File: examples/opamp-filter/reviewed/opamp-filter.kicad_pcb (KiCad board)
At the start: 2 copper layers, 80 x 45 mm, 19 parts, among them J1 IN, J2 5V, J3 OUT, U1 MCP6001R, U2 MCP6001R

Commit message: Regenerate the five with stitched pours, silk that speaks, and wires that never double back
All ten variants rebuilt by the fixed generator: reviewed boards carry
ground on both faces with the stitching ring (buck 35 vias, fpga 116),
thru_hole_only front pours, the board id and connector pin names in
silk, and the buck's explicit ground return; the sheets hook power up
through upright symbols and source-anchored flags with no overlapping
wires and no junction-less tees left. Every reviewed variant passes its
own gate with zero errors; every as-generated variant still fails, now
also for the rules this round added.

Co-Authored-By: Claude Fable 5 <noreply@anthropic.com>
Claude-Session: https://claude.ai/code/session_01DUj7Ltu92tWg159mCSacwY
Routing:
- net GND: vias 11 -> 33
- added copper zone on F.Cu, net GND
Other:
- board text added: "+5V"
- board text added: "GND"
- board text added: "IN"
- board text added: "OUT_AC"
- board text added: "opamp-filter rev A"
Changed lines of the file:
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@@
 	(via (at 154.0 76.6) (size 0.8) (drill 0.4) (layers "F.Cu" "B.Cu") (net 1))
 	(via (at 158.0 91.75) (size 0.8) (drill 0.4) (layers "F.Cu" "B.Cu") (net 1))
+	(via (at 104.5 64.5) (size 0.8) (drill 0.4) (layers "F.Cu" "B.Cu") (net 1))
+	(via (at 104.5 100.5) (size 0.8) (drill 0.4) (layers "F.Cu" "B.Cu") (net 1))
+	(via (at 114.5 64.5) (size 0.8) (drill 0.4) (layers "F.Cu" "B.Cu") (net 1))
+	(via (at 114.5 100.5) (size 0.8) (drill 0.4) (layers "F.Cu" "B.Cu") (net 1))
+	(via (at 124.5 64.5) (size 0.8) (drill 0.4) (layers "F.Cu" "B.Cu") (net 1))
+	(via (at 124.5 100.5) (size 0.8) (drill 0.4) (layers "F.Cu" "B.Cu") (net 1))
+	(via (at 134.5 64.5) (size 0.8) (drill 0.4) (layers "F.Cu" "B.Cu") (net 1))
+	(via (at 134.5 100.5) (size 0.8) (drill 0.4) (layers "F.Cu" "B.Cu") (net 1))
+	(via (at 144.5 64.5) (size 0.8) (drill 0.4) (layers "F.Cu" "B.Cu") (net 1))
+	(via (at 144.5 100.5) (size 0.8) (drill 0.4) (layers "F.Cu" "B.Cu") (net 1))
+	(via (at 154.5 64.5) (size 0.8) (drill 0.4) (layers "F.Cu" "B.Cu") (net 1))
+	(via (at 154.5 100.5) (size 0.8) (drill 0.4) (layers "F.Cu" "B.Cu") (net 1))
+	(via (at 164.5 64.5) (size 0.8) (drill 0.4) (layers "F.Cu" "B.Cu") (net 1))
+	(via (at 164.5 100.5) (size 0.8) (drill 0.4) (layers "F.Cu" "B.Cu") (net 1))
+	(via (at 174.5 64.5) (size 0.8) (drill 0.4) (layers "F.Cu" "B.Cu") (net 1))
+	(via (at 174.5 100.5) (size 0.8) (drill 0.4) (layers "F.Cu" "B.Cu") (net 1))
+	(via (at 104.5 74.5) (size 0.8) (drill 0.4) (layers "F.Cu" "B.Cu") (net 1))
+	(via (at 175.5 74.5) (size 0.8) (drill 0.4) (layers "F.Cu" "B.Cu") (net 1))
+	(via (at 104.5 84.5) (size 0.8) (drill 0.4) (layers "F.Cu" "B.Cu") (net 1))
+	(via (at 175.5 84.5) (size 0.8) (drill 0.4) (layers "F.Cu" "B.Cu") (net 1))
+	(via (at 104.5 94.5) (size 0.8) (drill 0.4) (layers "F.Cu" "B.Cu") (net 1))
+	(via (at 175.5 94.5) (size 0.8) (drill 0.4) (layers "F.Cu" "B.Cu") (net 1))
 	(zone
 		(net 1)
@@
 		(polygon (pts (xy 103.0 63.0) (xy 177.0 63.0) (xy 177.0 102.0) (xy 103.0 102.0)))
 	)
+	(zone
+		(net 1)
+		(net_name "GND")
+		(layer "F.Cu")
+		(hatch edge 0.5)
+		(connect_pads thru_hole_only
+			(clearance 0.4)
+		)
+		(min_thickness 0.175)
+		(filled_areas_thickness no)
+		(fill yes
+			(thermal_gap 0.5)
+			(thermal_bridge_width 0.5)
+		)
+		(polygon (pts (xy 103.0 63.0) (xy 177.0 63.0) (xy 177.0 102.0) (xy 103.0 102.0)))
+	)
+	(gr_text "opamp-filter rev A" (at 140.0 102.8 0) (layer "F.SilkS") (effects (font (size 1.0 1.0) (thickness 0.15))))
+	(gr_text "IN" (at 111.37 78.0 0) (layer "F.SilkS") (effects (font (size 0.8 0.8) (thickness 0.12))))
+	(gr_text "GND" (at 111.37 80.54 0) (layer "F.SilkS") (effects (font (size 0.8 0.8) (thickness 0.12))))
+	(gr_text "OUT_AC" (at 168.63 78.0 0) (layer "F.SilkS") (effects (font (size 0.8 0.8) (thickness 0.12))))
+	(gr_text "GND" (at 168.63 80.54 0) (layer "F.SilkS") (effects (font (size 0.8 0.8) (thickness 0.12))))
+	(gr_text "+5V" (at 170.0 74.3 0) (layer "F.SilkS") (effects (font (size 0.8 0.8) (thickness 0.12))))
+	(gr_text "GND" (at 175.0 74.3 0) (layer "F.SilkS") (effects (font (size 0.8 0.8) (thickness 0.12))))
 )

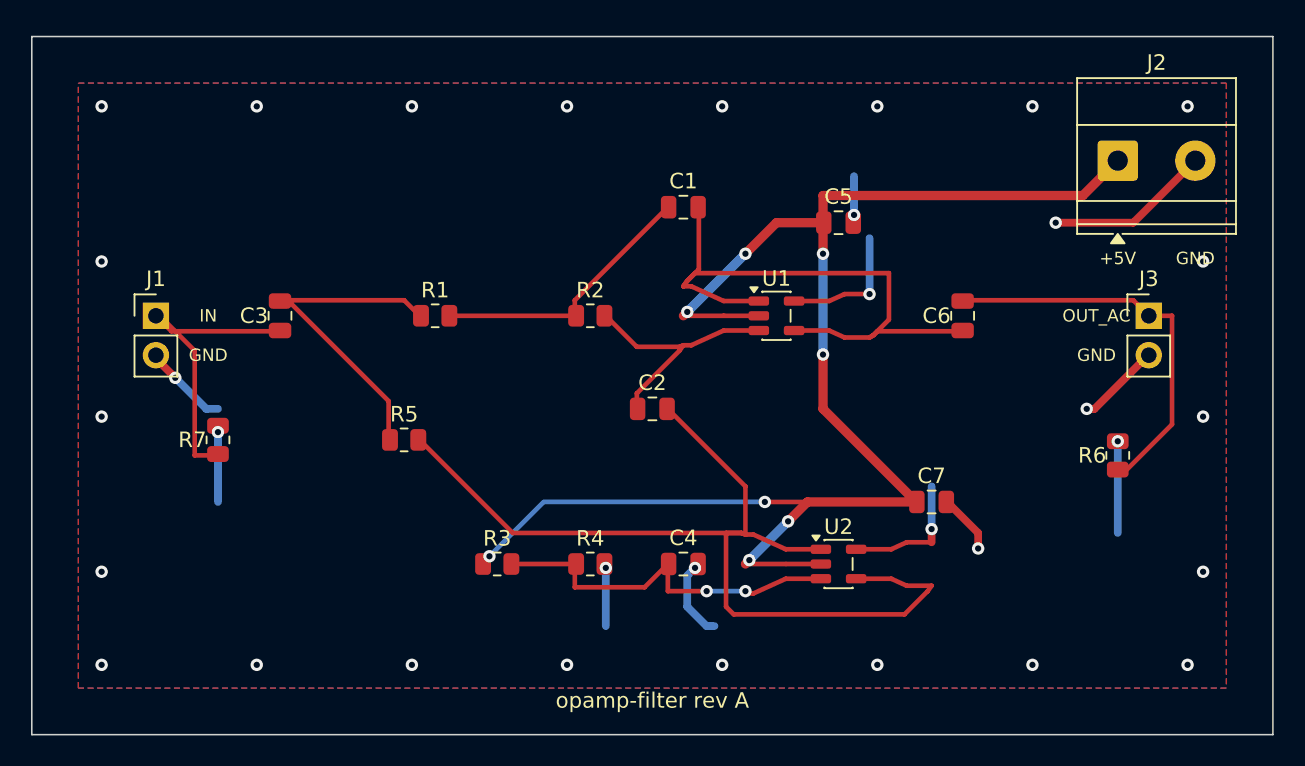
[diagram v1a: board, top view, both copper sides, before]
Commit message: Regenerate the five as round three drew them
All five reviewed projects pass their gates again: the buck all wire
with its feedback drawn home, the motor's logic named at the header,
the carrier reading as the pinout table it is - with its feed diode
finally pointing the right way - the filter compact with test points,
and the FPGA's capacitors sitting beside the units they feed. Thirty
renders redrawn, verdict tables at today's numbers.

Co-Authored-By: Claude Fable 5 <noreply@anthropic.com>
Claude-Session: https://claude.ai/code/session_01DUj7Ltu92tWg159mCSacwY
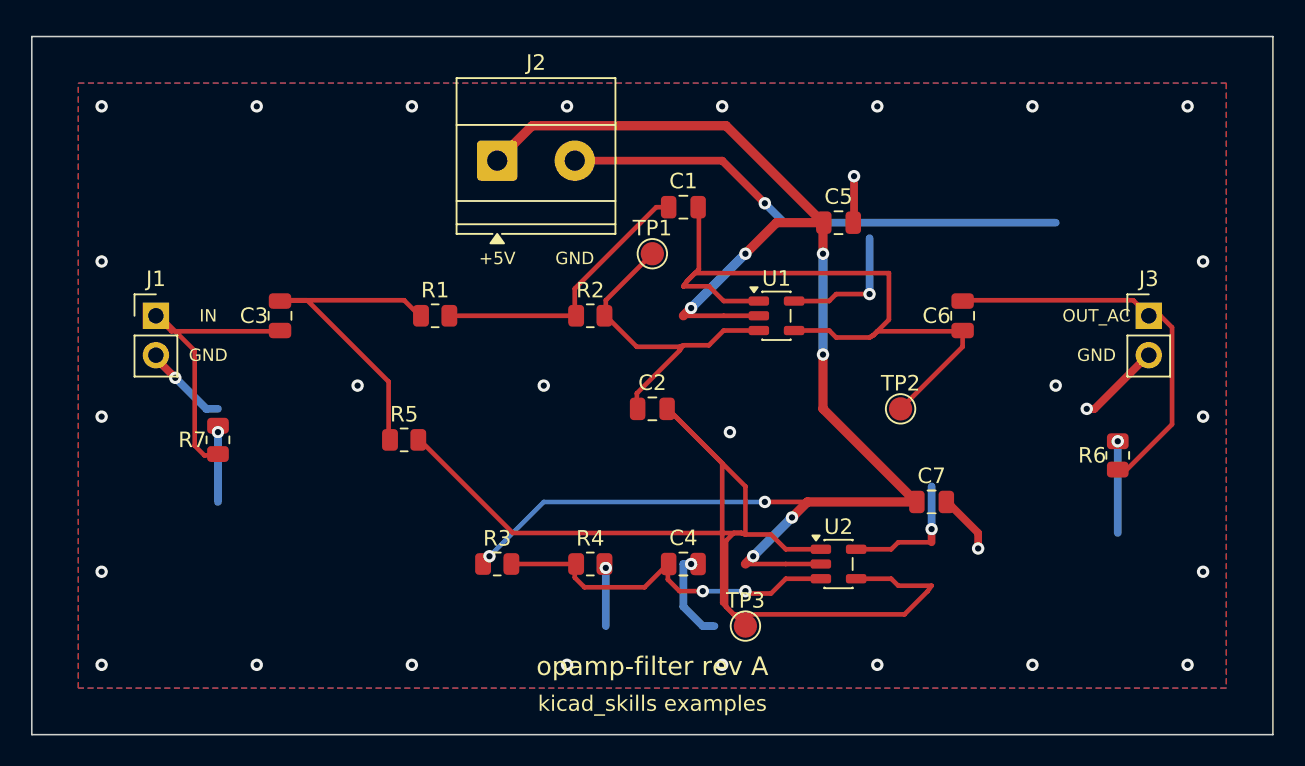
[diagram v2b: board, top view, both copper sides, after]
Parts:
- added TP1: TP, TestPoint:TestPoint_Pad_D1.5mm, F.Cu at (140.0, 74.0)
- added TP2: TP, TestPoint:TestPoint_Pad_D1.5mm, F.Cu at (156.0, 84.0)
- added TP3: TP, TestPoint:TestPoint_Pad_D1.5mm, F.Cu at (146.0, 98.0)
- moved J2 40.0 mm to (130.0, 68.0)
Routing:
- net GND: track 65.8 -> 88.9 mm, vias 33 -> 37
- net /VREF: track 64.1 -> 80.2 mm
- net /OUT: track 40.0 -> 47.0 mm
- net /FILT_IN: track 16.3 -> 21.8 mm
- net +5V: track 105.8 -> 108.7 mm
- net /IN_DC: track 21.7 -> 22.4 mm
- net /MID: track 24.3 -> 23.7 mm
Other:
- board text added: "kicad_skills examples"

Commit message: Regenerate the four boards round four has settled
The buck, the motor driver, the carrier and the filter as the current
generator draws them: interior ground stitching on all four, the motor
driver's bundle tight and its board twelve millimetres shorter, the
filter compact and hand-placed, the carrier's indicator in a column of
its own. All four pass their gates. The FPGA is still regenerating.

Co-Authored-By: Claude Fable 5 <noreply@anthropic.com>
Claude-Session: https://claude.ai/code/session_01DUj7Ltu92tWg159mCSacwY
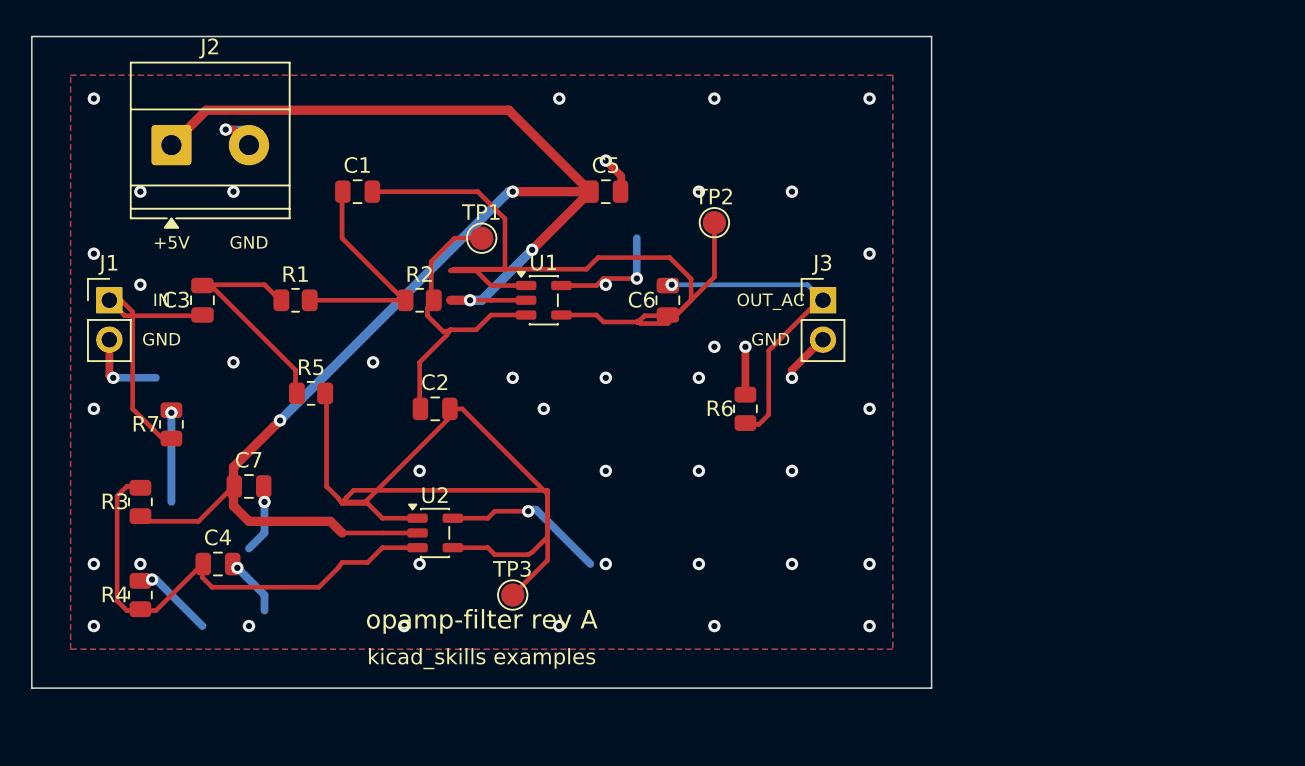
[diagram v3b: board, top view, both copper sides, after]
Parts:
- moved C7 44.0 mm to (114.0, 89.0)
- moved C4 30.0 mm to (112.0, 94.0)
- moved R4 29.1 mm to (107.0, 96.0), turned to 90 degrees
- moved U2 26.1 mm to (126.0, 92.0)
- moved R6 24.2 mm to (146.0, 84.0)
- moved R3 23.3 mm to (107.0, 90.0), turned to 90 degrees
- moved C1 21.0 mm to (121.0, 70.0)
- moved J2 21.0 mm to (109.0, 67.0)
- moved J3 21.0 mm to (151.0, 77.0)
- moved C6 19.0 mm to (141.0, 77.0)
- moved TP2 17.0 mm to (144.0, 72.0)
- moved C5 15.1 mm to (137.0, 70.0)
- moved TP3 15.1 mm to (131.0, 96.0)
- moved U1 15.0 mm to (133.0, 77.0)
- moved C2 14.0 mm to (126.0, 84.0)
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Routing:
- net GND: track 88.9 -> 55.2 mm, vias 37 -> 49
- net /VREF: track 80.2 -> 62.0 mm
- net /OUT: track 47.0 -> 58.0 mm
- net +5V: track 108.7 -> 99.6 mm, vias 8 -> 4
- net /MID: track 23.7 -> 31.7 mm, vias 2 -> 0
- net /IN_DC: track 22.4 -> 15.3 mm
- net /OUT_AC: track 25.2 -> 21.2 mm, vias 0 -> 1
- net /X: track 18.2 -> 14.9 mm
- net /IN: track 19.7 -> 17.8 mm
- net /FILT_IN: track 21.8 -> 20.7 mm
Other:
- board size 80 x 45 mm -> 58 x 42 mm

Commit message: Regenerate the four boards whose corners were off the grid
Ninety-one bends at angles nobody chose, now none. All four still pass
their gates.

Co-Authored-By: Claude Fable 5 <noreply@anthropic.com>
Claude-Session: https://claude.ai/code/session_01DUj7Ltu92tWg159mCSacwY
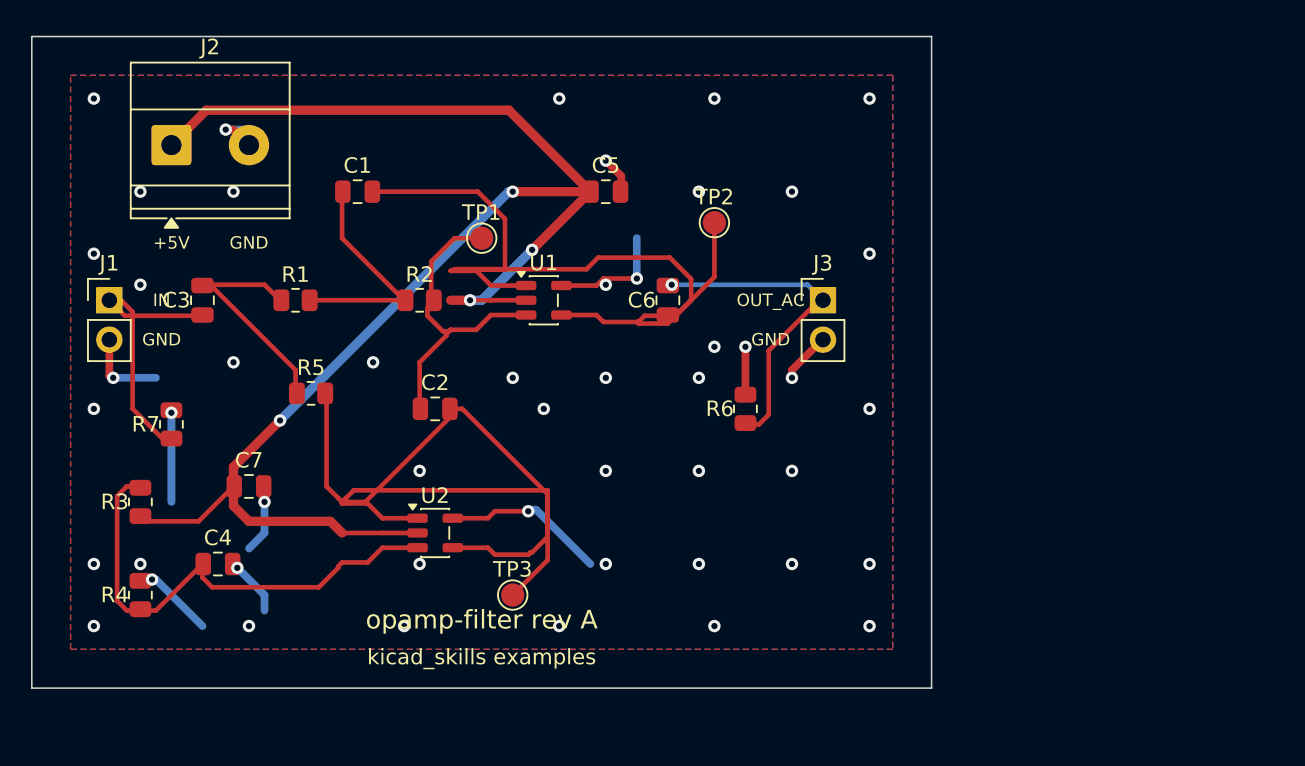
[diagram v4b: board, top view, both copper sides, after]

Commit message: Regenerate the four the text and width work changed
Designators and values off the rails they were printed on, power-named
nets at the width their rule asks for, and the buck's feedback ending
on the capacitor pad it senses at.

Co-Authored-By: Claude Fable 5 <noreply@anthropic.com>
Claude-Session: https://claude.ai/code/session_01DUj7Ltu92tWg159mCSacwY
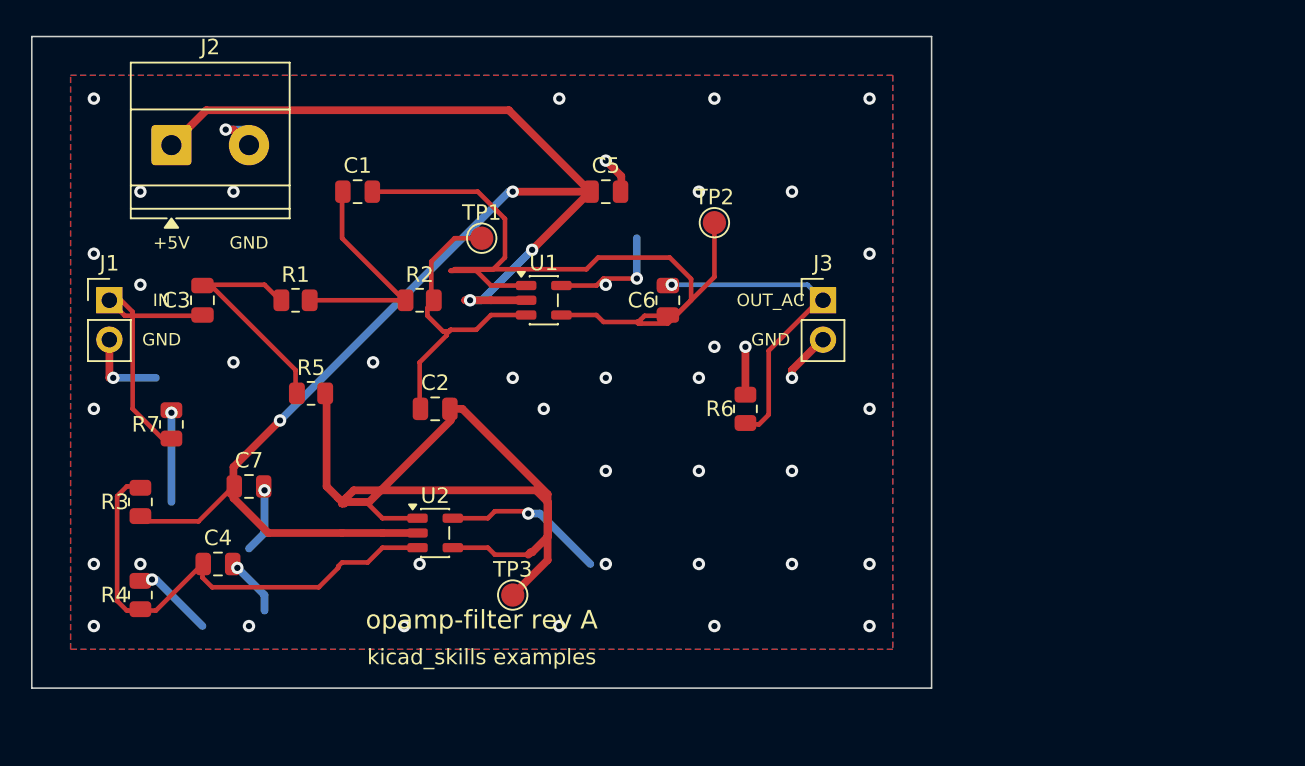
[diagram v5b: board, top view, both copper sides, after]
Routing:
- net +5V: track 99.6 -> 97.5 mm
- net /IN: track 17.9 -> 17.0 mm
- net GND: track 55.3 -> 55.4 mm, vias 49 -> 48
